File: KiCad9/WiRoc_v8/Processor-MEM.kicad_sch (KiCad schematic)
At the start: 30 parts, among them U11 AllwinnerH3, U12 DDR3

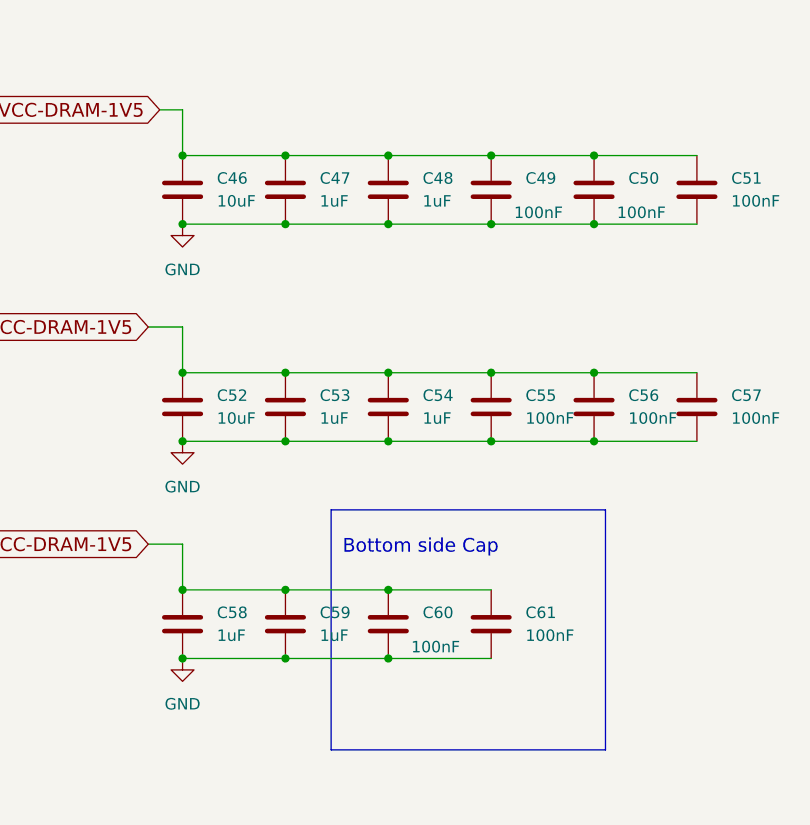
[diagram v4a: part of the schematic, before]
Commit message: change to 10uF in pdn, vdd-dram area to south caps, remove varistor, etc
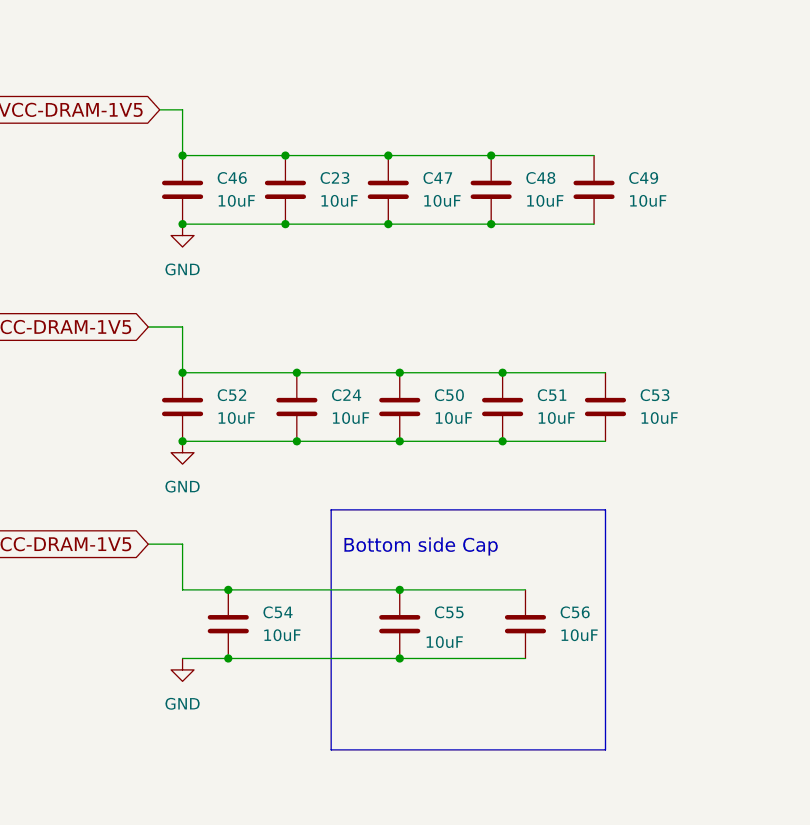
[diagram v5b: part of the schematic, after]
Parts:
- removed C57, C60, C61: 100nF, Capacitor_SMD:C_0402_1005Metric, symbol Device:C
- removed C58, C59: 1uF, Capacitor_SMD:C_0402_1005Metric, symbol Device:C
- added C23, C24: 10uF, Capacitor_SMD:C_0402_1005Metric, symbol Device:C
- C47, C48, C53, C54: value 1uF -> 10uF; LCSC Part # C52923 -> C15525; ManufacturerPartNumber CL05A105KA5NQNC -> CL05A106MQ5NUNC
- C49, C50, C51, C55, C56: value 100nF -> 10uF; LCSC Part # C1525 -> C15525; ManufacturerPartNumber CL05B104KO5NNNC -> CL05A106MQ5NUNC
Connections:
- net GND: now also C23.2, C24.2
- net VCC-DRAM-1V5: now also C23.1, C24.1

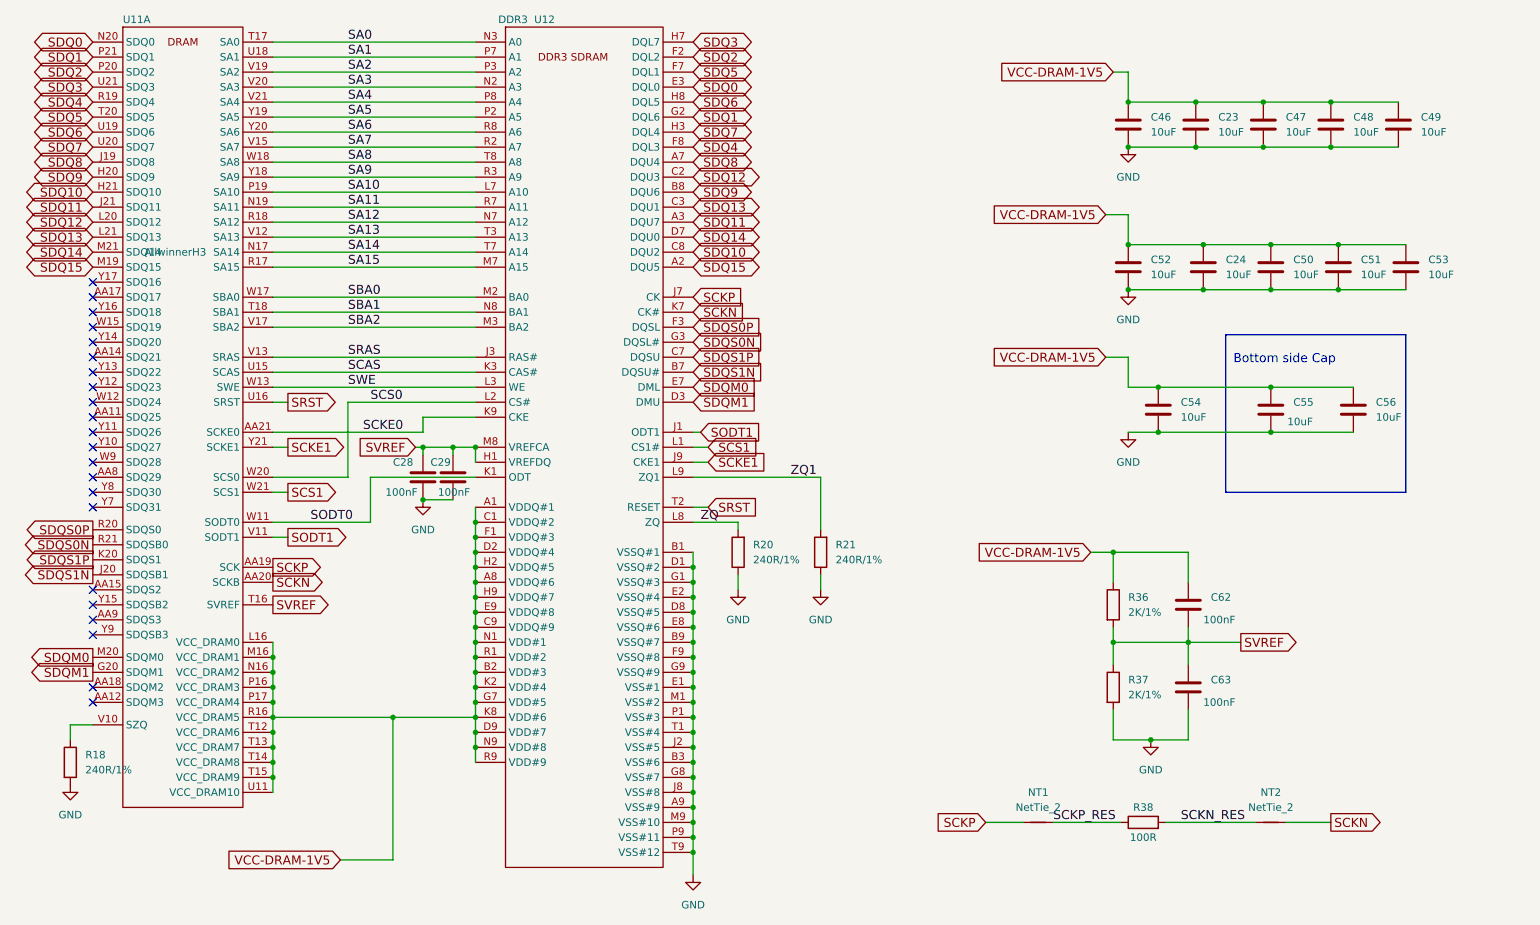
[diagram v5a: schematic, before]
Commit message: shorten spi meander, dataready/handshake shouldn't be length matched to spi. Move eMMC-cmd pullup to processor via. Make meanders more spacious.
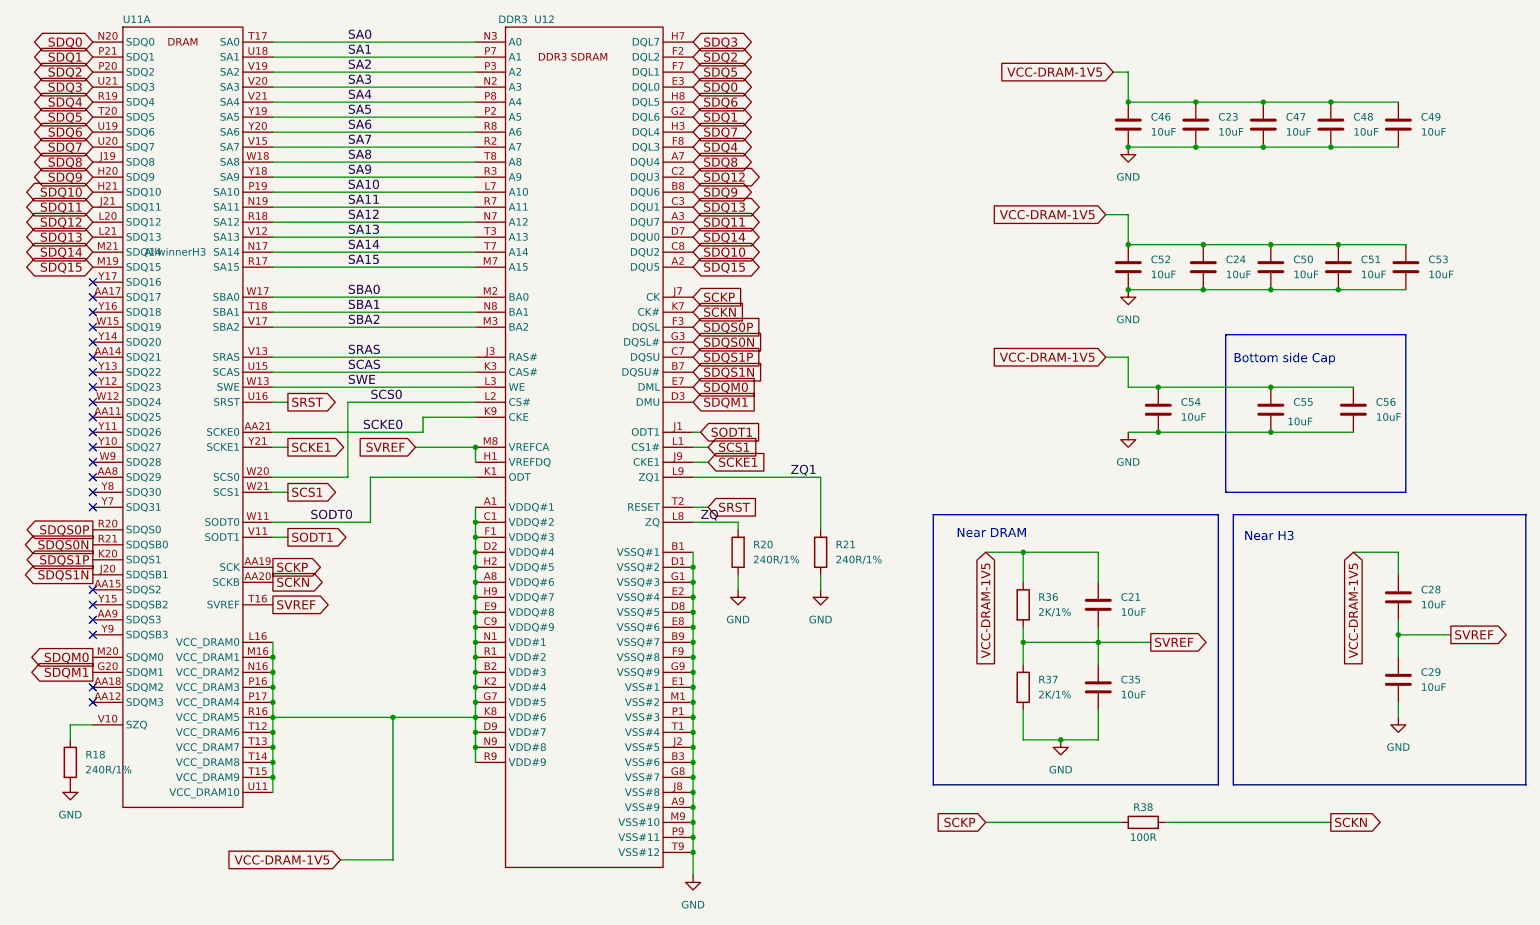
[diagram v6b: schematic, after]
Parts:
- removed C62, C63: 100nF, Capacitor_SMD:C_0402_1005Metric, symbol Device:C
- removed NT1, NT2: NetTie_2, WiRoc:NetTie-2_SMD_Pad0.12mm, symbol Device:NetTie_2
- added C21, C35: 10uF, Capacitor_SMD:C_0402_1005Metric, symbol Device:C
- C28, C29: value 100nF -> 10uF; LCSC Part # C1525 -> C15525; ManufacturerPartNumber CL05B104KO5NNNC -> CL05A106MQ5NUNC
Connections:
- net SCKN_RES is gone; now on net SCKN: R38.2
- net SCKP_RES is gone; now on net SCKP: R38.1
- net GND: now also C35.2; no longer C28.2
- net SVREF: now also C28.2, C21.2, C35.1; no longer C28.1
- net VCC-DRAM-1V5: now also C28.1, C21.1
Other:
- note added: "Near DRAM"
- note added: "Near H3"
- moved on the sheet: R36, R37

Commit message: many small changes, change eMMC
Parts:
- C21, C23, C24, C28, C29, C35, C46, C47, C48, C49, C50, C51, C52, C53, C54, C55, C56: value 10uF -> 10uF/6.3V
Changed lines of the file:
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@@
 			)
 		)
-		(property "Value" "10uF"
+		(property "Value" "10uF/6.3V"
 			(at 245.11 44.45 0)
 			(effects
@@
 			)
 		)
-		(property "Value" "10uF"
+		(property "Value" "10uF/6.3V"
 			(at 256.54 124.46 0)
 			(effects
@@
 			)
 		)
-		(property "Value" "10uF"
+		(property "Value" "10uF/6.3V"
 			(at 246.38 68.58 0)
 			(effects
@@
 			)
 		)
-		(property "Value" "10uF"
+		(property "Value" "10uF/6.3V"
 			(at 210.82 68.58 0)
 			(effects
@@
 			)
 		)
-		(property "Value" "10uF"
+		(property "Value" "10uF/6.3V"
 			(at 205.74 125.73 0)
 			(effects
@@
 			)
 		)
-		(property "Value" "10uF"
+		(property "Value" "10uF/6.3V"
 			(at 215.9 92.71 0)
 			(effects
@@
 			)
 		)
-		(property "Value" "10uF"
+		(property "Value" "10uF/6.3V"
 			(at 257.81 68.58 0)
 			(effects
@@
 			)
 		)
-		(property "Value" "10uF"
+		(property "Value" "10uF/6.3V"
 			(at 210.82 44.45 0)
 			(effects
@@
 			)
 		)
-		(property "Value" "10uF"
+		(property "Value" "10uF/6.3V"
 			(at 248.92 92.71 0)
 			(effects
@@
 			)
 		)
-		(property "Value" "10uF"
+		(property "Value" "10uF/6.3V"
 			(at 256.54 44.45 0)
 			(effects
@@
 			)
 		)
-		(property "Value" "10uF"
+		(property "Value" "10uF/6.3V"
 			(at 256.54 138.43 0)
 			(effects
@@
 			)
 		)
-		(property "Value" "10uF"
+		(property "Value" "10uF/6.3V"
 			(at 222.25 44.45 0)
 			(effects
@@
 			)
 		)
-		(property "Value" "10uF"
+		(property "Value" "10uF/6.3V"
 			(at 234.95 68.58 0)
 			(effects
@@
 			)
 		)
-		(property "Value" "10uF"
+		(property "Value" "10uF/6.3V"
 			(at 223.52 68.58 0)
 			(effects
@@
 			)
 		)
-		(property "Value" "10uF"
+		(property "Value" "10uF/6.3V"
 			(at 233.934 93.472 0)
 			(effects
@@
 			)
 		)
-		(property "Value" "10uF"
+		(property "Value" "10uF/6.3V"
 			(at 233.68 44.45 0)
 			(effects
@@
 			)
 		)
-		(property "Value" "10uF"
+		(property "Value" "10uF/6.3V"
 			(at 205.74 139.7 0)
 			(effects

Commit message: etc
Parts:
- U12: footprint Package_BGA:BGA-96_9.0x13.0mm_Layout2x3x16_P0.8mm -> WiRoc:BGA-96_8.0x14.0mm_Layout2x3x16_P0.8mm
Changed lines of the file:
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@@
 			)
 		)
-		(property "Footprint" "Package_BGA:BGA-96_9.0x13.0mm_Layout2x3x16_P0.8mm"
+		(property "Footprint" "WiRoc:BGA-96_8.0x14.0mm_Layout2x3x16_P0.8mm"
 			(at 102.87 25.4 0)
 			(effects
